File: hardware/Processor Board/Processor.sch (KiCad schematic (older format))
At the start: 14 parts, among them IC1 74HC00, IC2 W65C02, IC4 SYSTEM ROM, IC5 RAM, SW1 ~NMI, X1 BUS

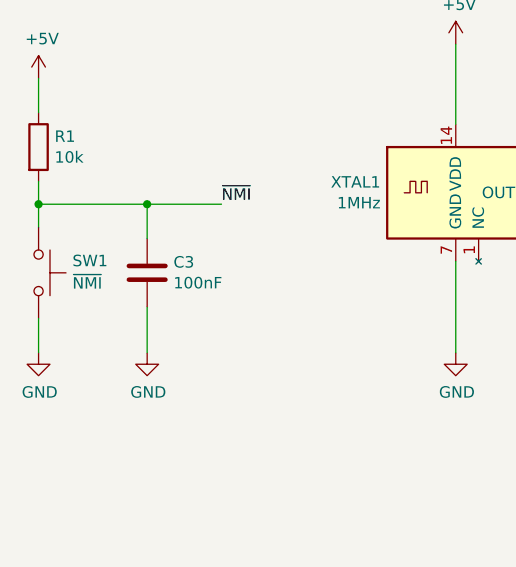
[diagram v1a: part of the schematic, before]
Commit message: Rename NMI push button
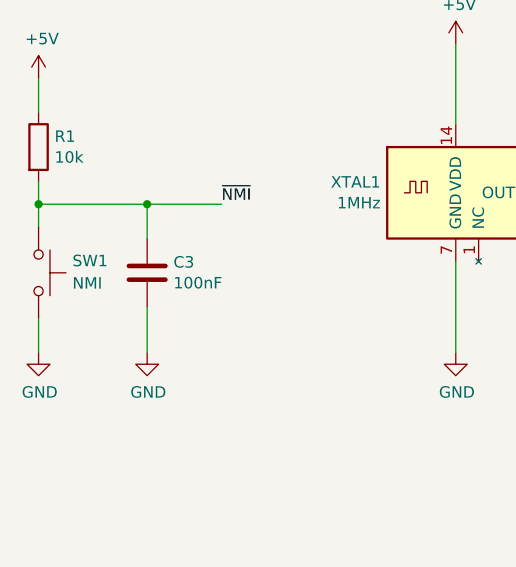
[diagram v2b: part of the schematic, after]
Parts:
- SW1: value ~NMI -> NMI
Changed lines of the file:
@@
 P 925 1825
 F 0 "SW1" V 873 1973 50  0000 L CNN
-F 1 "~NMI" V 971 1973 50  0000 L CNN
+F 1 "NMI" V 971 1973 50  0000 L CNN
 F 2 "Button_Switch_THT:SW_Tactile_SPST_Angled_PTS645Vx83-2LFS" H 925 2025 50  0001 C CNN
 F 3 "https://www.mouser.de/datasheet/2/60/CK-Components-1131575.pdf" H 925 2025 50  0001 C CNN

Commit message: Working on hardware
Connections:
- net RDY: now also X1.20 (Pin_20); no longer X1.26 (Pin_26)
- net SYNC: now also X1.24 (Pin_24); no longer X1.28 (Pin_28)
- net ~IRQ: now also X1.18 (Pin_18); no longer X1.22 (Pin_22)
- net ~NMI: now also X1.22 (Pin_22); no longer X1.24 (Pin_24)
- net CLOCK_OSC renamed CLOCK
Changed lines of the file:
@@
 	5050 7675 5050 7775
 Text Label 3250 1475 0    50   ~ 0
-CLOCK_OSC
+CLOCK
 Wire Wire Line
 	3250 1475 3150 1475
@@
 	14375 6825 14775 6825
 Wire Wire Line
-	14475 5925 14375 5925
-Wire Wire Line
-	14475 6025 14375 6025
+	14475 5725 14375 5725
+Wire Wire Line
+	14475 5825 14375 5825
 NoConn ~ 14375 6725
 NoConn ~ 14375 6625
@@
 NoConn ~ 14375 6425
 Wire Wire Line
-	14475 6125 14375 6125
+	14475 5925 14375 5925
 Wire Bus Line
 	11550 4725 11550 7125
@@
 Text Label 13775 6525 2    50   ~ 0
 R~W
-Text Label 13800 6725 2    50   ~ 0
+Text Label 13775 6725 2    50   ~ 0
 ~RESET
 Wire Wire Line
-	13875 6725 13800 6725
-Text Label 14475 5925 0    50   ~ 0
+	13875 6725 13775 6725
+Text Label 14475 5725 0    50   ~ 0
 ~IRQ
-Text Label 14475 6125 0    50   ~ 0
+Text Label 14475 5825 0    50   ~ 0
 RDY
-Text Label 14475 6225 0    50   ~ 0
+Text Label 14475 6025 0    50   ~ 0
 SYNC
 NoConn ~ 14375 6325
@@
 	1725 1525 1400 1525
 Connection ~ 1400 1525
-Text Label 14475 6025 0    50   ~ 0
+Text Label 14475 5925 0    50   ~ 0
 ~NMI
 Wire Wire Line
-	14375 6225 14475 6225
+	14375 6025 14475 6025
 Wire Wire Line
 	13775 6525 13875 6525
 Text Label 5875 4325 0    50   ~ 0
-CLOCK_OSC
+CLOCK
 Text Label 8150 7475 2    50   ~ 0
-CLOCK_OSC
-Text Label 13800 6625 2    50   ~ 0
-CLOCK_OSC
-NoConn ~ 14375 5725
-NoConn ~ 14375 5825
-Wire Wire Line
-	13800 6625 13875 6625
+CLOCK
+Text Label 13775 6625 2    50   ~ 0
+CLOCK
+Wire Wire Line
+	13775 6625 13875 6625
 Wire Bus Line
 	11400 4625 14825 4625
@@
 Entry Wire Line
 	13475 5125 13375 5025
+NoConn ~ 14375 6125
+NoConn ~ 14375 6225
 Wire Bus Line
 	4150 7125 4150 8225
